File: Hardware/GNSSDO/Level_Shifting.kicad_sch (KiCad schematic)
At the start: 54 parts, among them J12 SMA_Edge, J3 SMA_Edge, SW4 DPDT_Slide_SMD_7.2x3.5mm, U10 74LVC2T45DC, U12 74LVC2T45DC, U16 74LVC2T45DC, U18 PCA9306, U8 74LVC2T45DC, U9 74LVC2T45DC

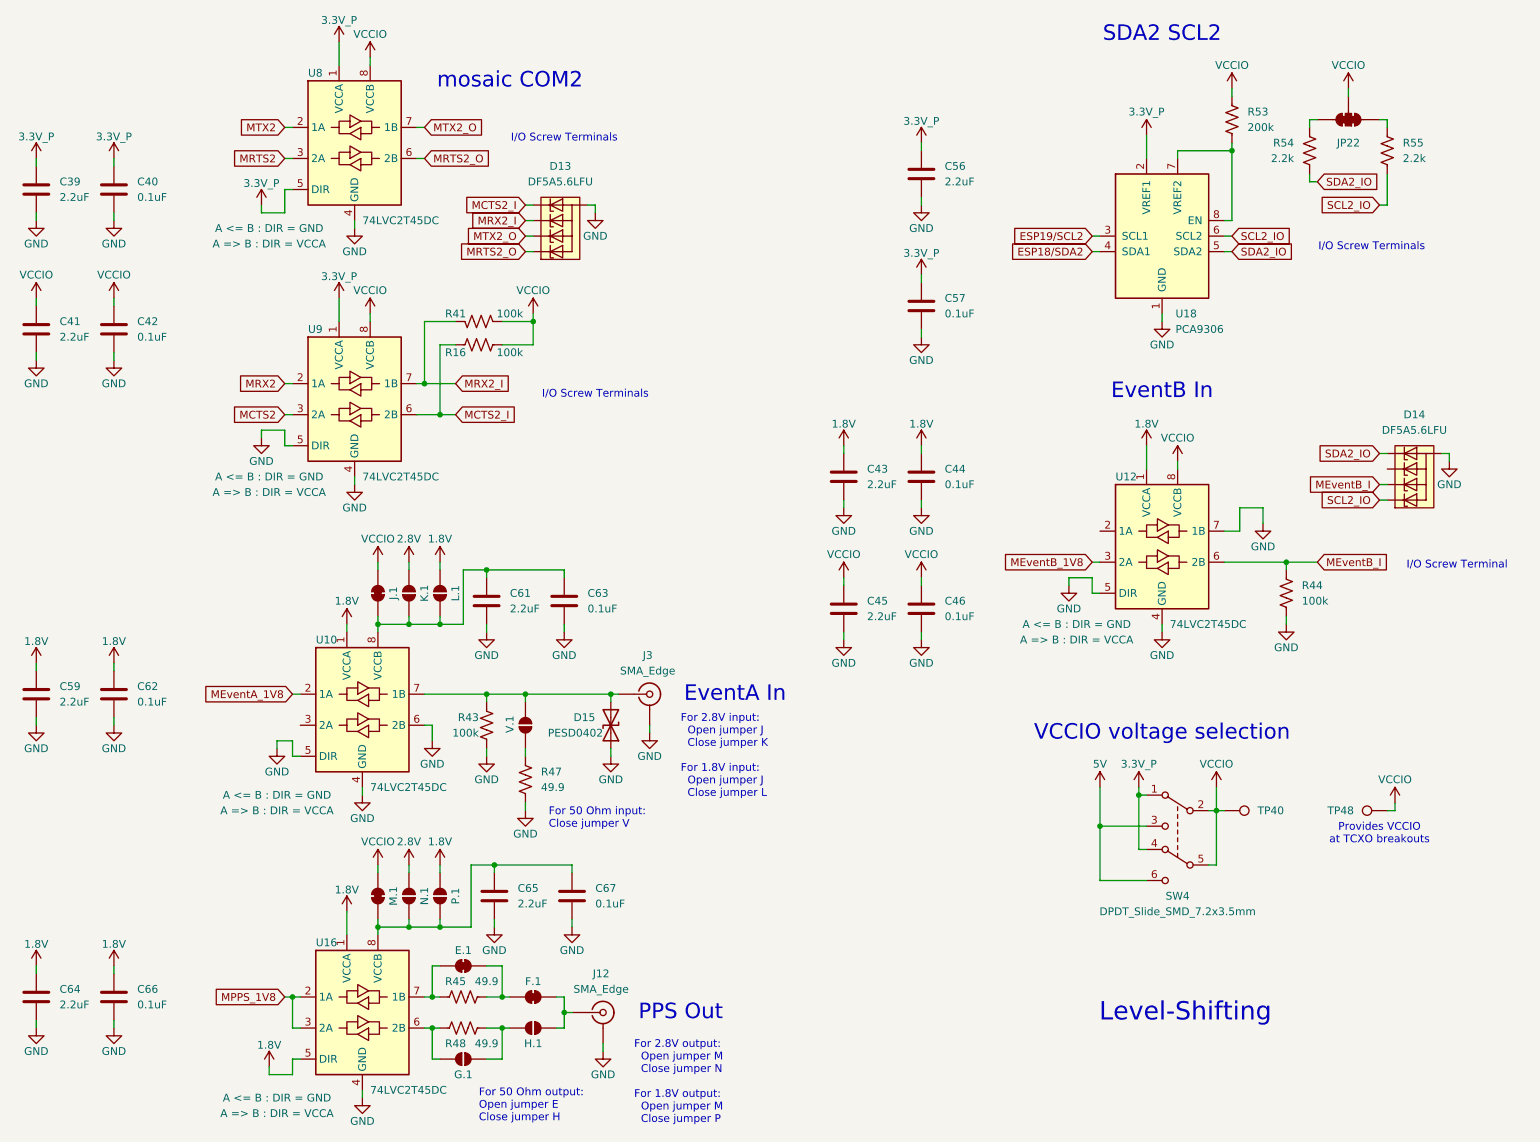
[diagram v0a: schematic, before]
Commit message: KiCad 10
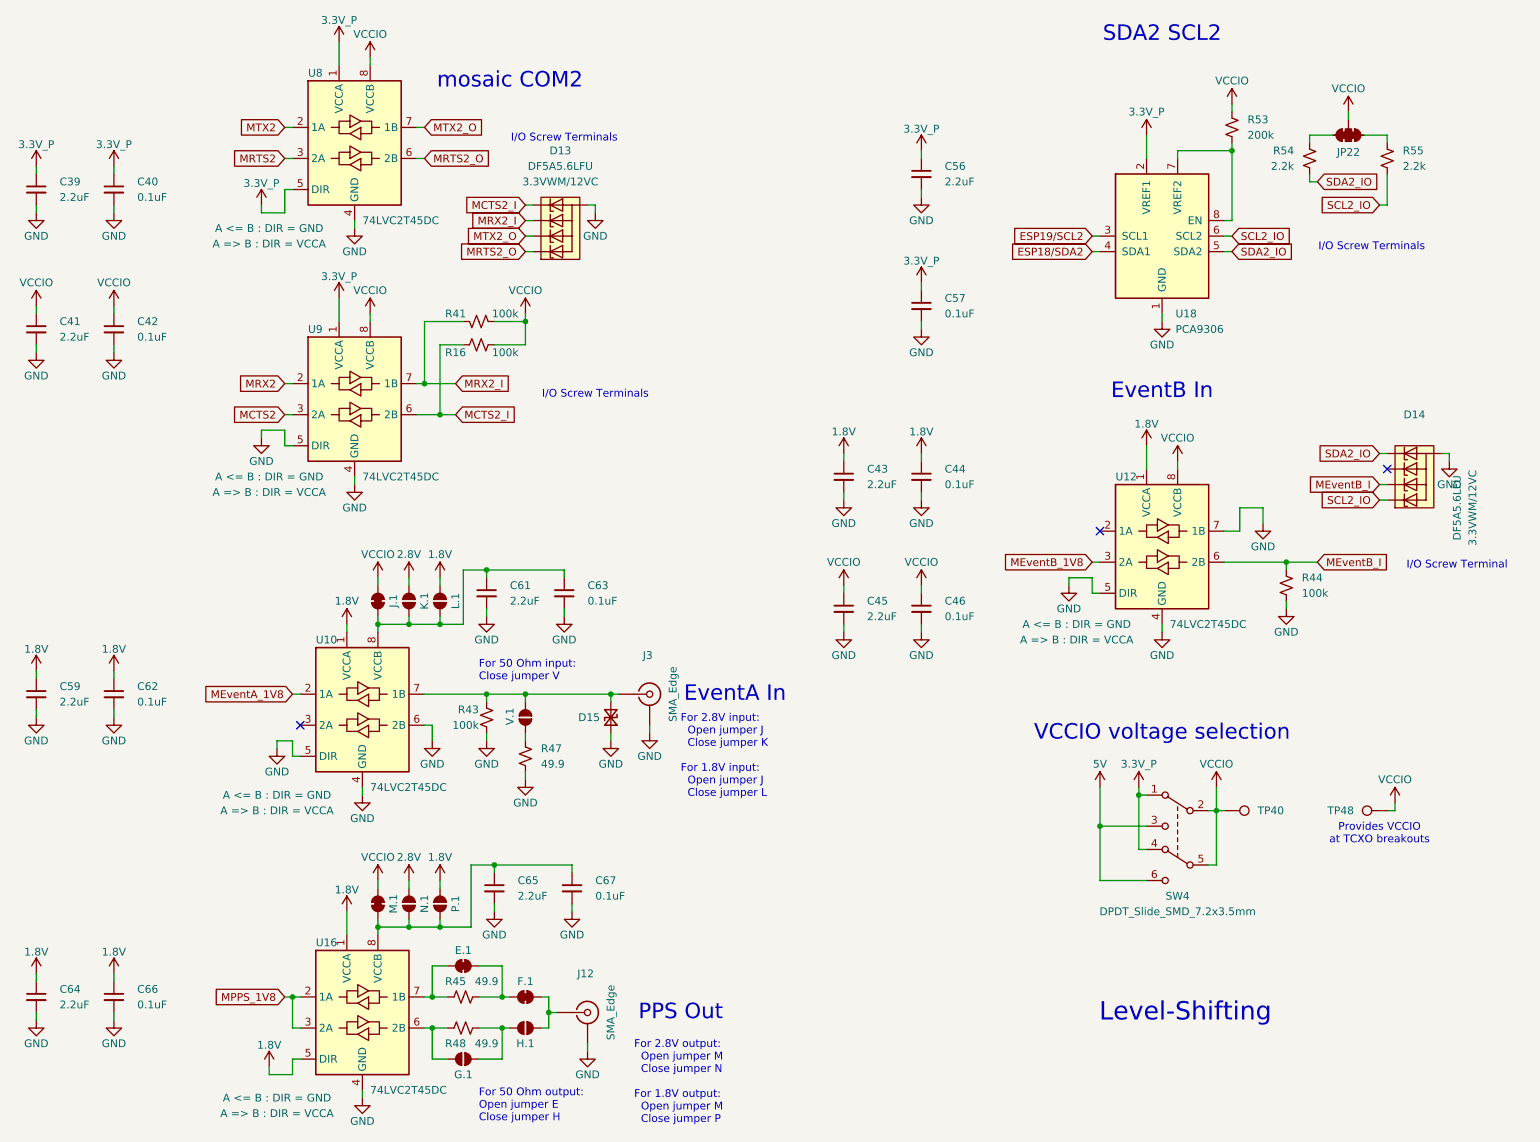
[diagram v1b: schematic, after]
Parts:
- C39, C41, C43, C45, C56, C59, C61, C64, C65: PROD_ID CAP-07888 -> CAP-24999
- D13, D14: symbol SparkFun-DiscreteSemi:D_TVS_ESD_4_HS -> SparkFun-DiscreteSemi:D_TVS_ESD_4_HS_3.3V; Rating (none) -> 3.3VWM/12VC
- D15: symbol SparkFun-DiscreteSemi:D_TVS_0402 -> SparkFun-DiscreteSemi:D_TVS_0402_14V; Rating (none) -> 14VWM/40VC
- E.1, F.1, G.1, H.1, J.1, JP22, K.1, L.1, M.1, N.1, P.1, V.1: value ~ -> (none)
- J12, J3: footprint SparkFun-Connector:SMA_Edge -> SparkFun-Connector:SMA_Edge_6.3mm; symbol SparkFun-RF:SMA_EdgeMount -> SparkFun-RF:SMA_EdgeMount_6.3mm
- TP40, TP48: footprint SparkFun-Connector:1x01 -> SparkFun-Connector:1x01_P2.54mm
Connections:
- net GND: now also R43.1, R44.1, R47.2; no longer R43.2, R44.2, R47.1
- net MCTS2_I: now also R16.1; no longer R16.2
- net MEventB_I: now also R44.2; no longer R44.1
- net MRX2_I: now also R41.1; no longer R41.2
- net SCL2_IO: now also R55.2; no longer R55.1
- net SDA2_IO: now also R54.2; no longer R54.1
- net VCCIO: now also R16.2, R41.2, R53.1; no longer R16.1, R41.1, R53.2
- net at V.1.1 (A): now also R47.1; no longer R47.2
- net at D15.2 (A2), J3.1 (In), U10.7 (1B)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: now also R43.2; no longer R43.1
- net at E.1.2 (B), F.1.1 (A): now also R45.2; no longer R45.1
- net at E.1.1 (A), U16.7 (1B): now also R45.1; no longer R45.2
- net at G.1.2 (B), H.1.1 (A): now also R48.2; no longer R48.1
- net at G.1.1 (A), U16.6 (2B): now also R48.1; no longer R48.2
- net at JP22.1 (A): now also R55.1; no longer R55.2
- net at U18.7 (VREF2), U18.8 (EN): now also R53.2; no longer R53.1
- net at JP22.3 (C): now also R54.1; no longer R54.2
- no-connect marks 0 -> 3
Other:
- moved on the sheet: C61, C63, C65, C67, D15, F.1, H.1, J.1, J12, JP22, K.1, L.1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
